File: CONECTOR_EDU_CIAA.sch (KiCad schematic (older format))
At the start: 2 parts

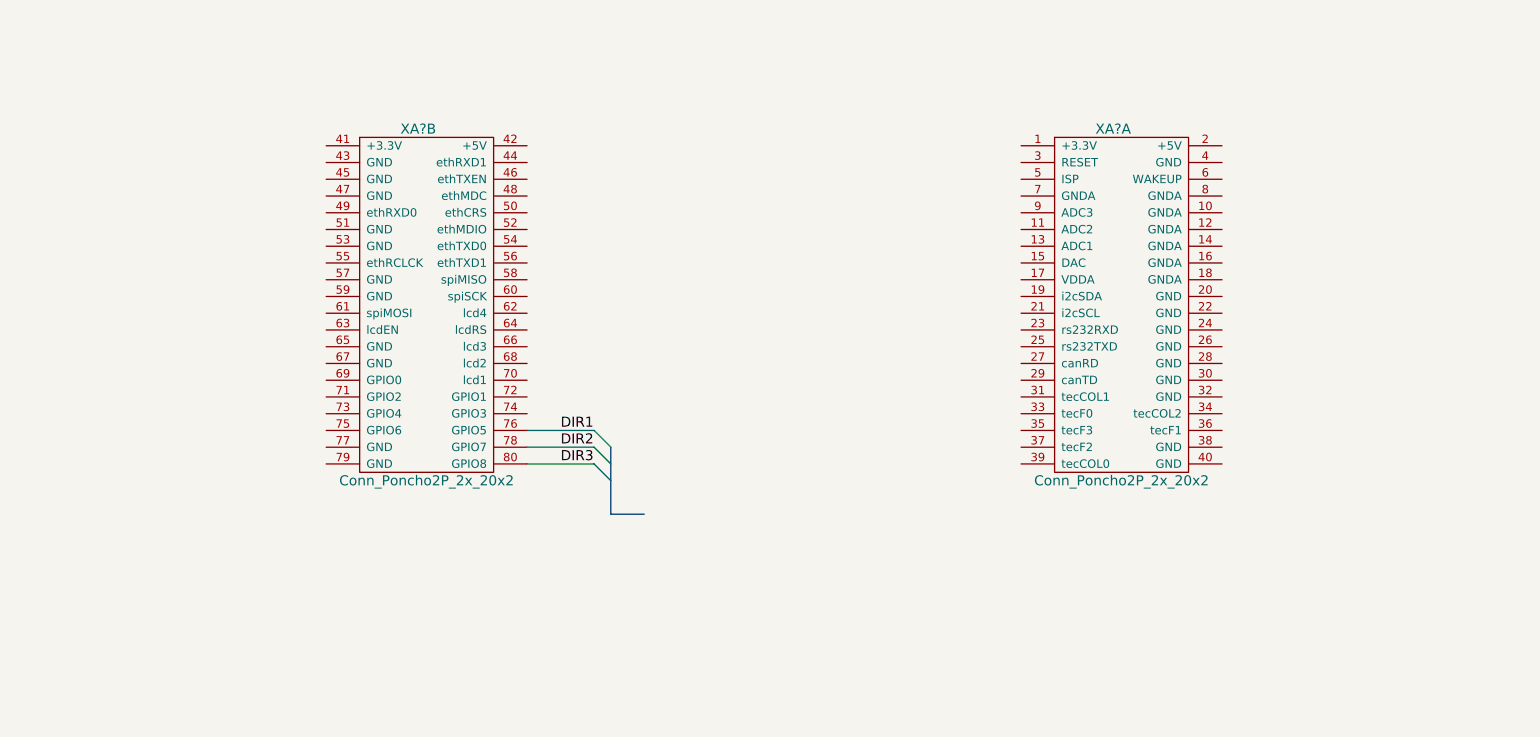
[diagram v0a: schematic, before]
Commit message: Adicion de documentacion
Creacion y adicion de componente A4988 en hoja POLOLUS_AXIS.sch, Avance parcialmente completo de  hoja POLOLUS_AXIS.sch
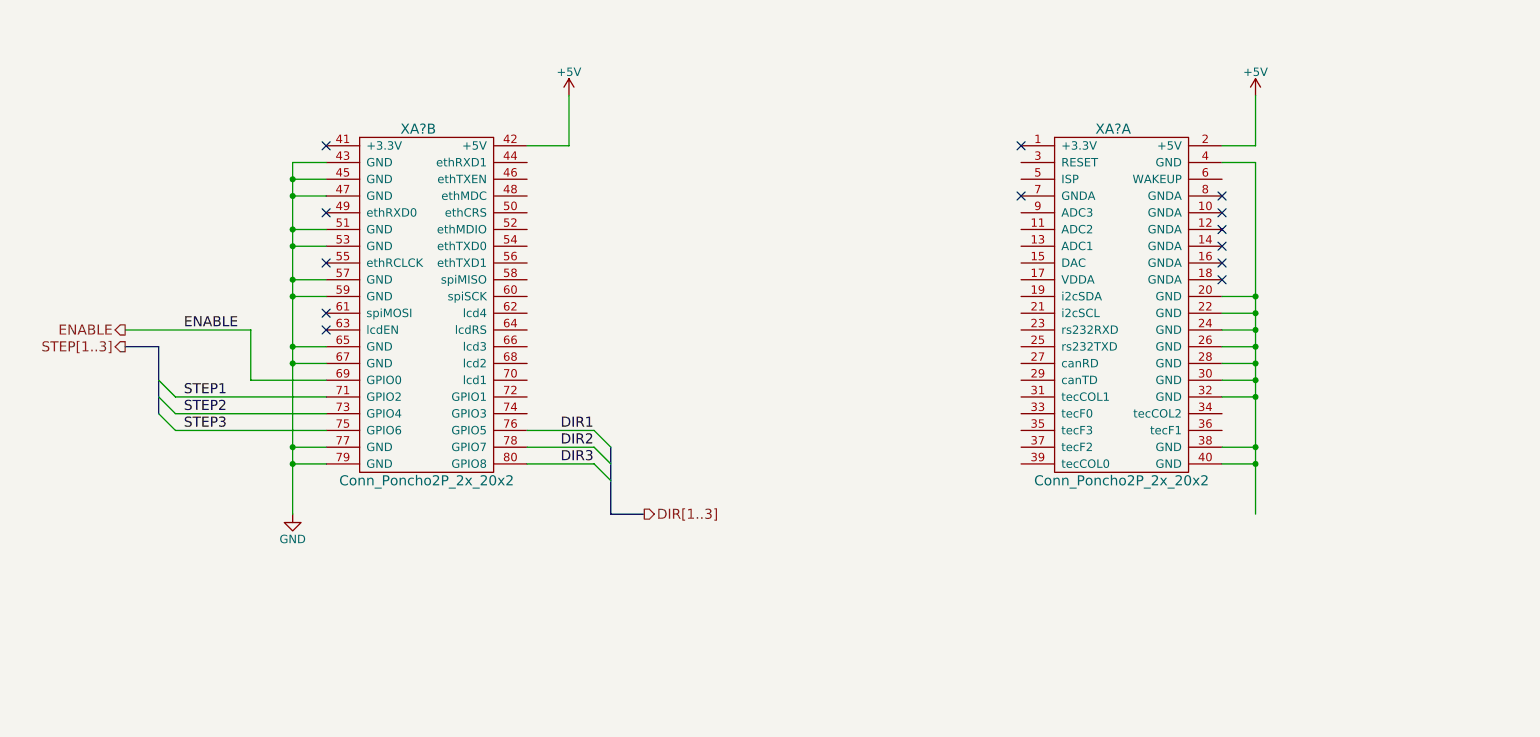
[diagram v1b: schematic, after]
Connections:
- net +5V: now reaches XA?.2 (+5V)
- net +5V: now also XA?.42 (+5V)
- net at XA?.20 (GND): now also XA?.22 (GND), XA?.24 (GND), XA?.26 (GND), XA?.28 (GND), XA?.30 (GND), XA?.32 (GND), XA?.38 (GND), XA?.4 (GND), XA?.40 (GND)
- net GND: now reaches XA?.43 (GND)
- net GND: now also XA?.45 (GND), XA?.47 (GND), XA?.51 (GND), XA?.53 (GND), XA?.57 (GND), XA?.59 (GND), XA?.65 (GND), XA?.67 (GND), XA?.77 (GND), XA?.79 (GND)
- net ENABLE: now reaches XA?.69 (GPIO0)
- net STEP1: now reaches XA?.71 (GPIO2)
- net STEP2: now reaches XA?.73 (GPIO4)
- net STEP3: now reaches XA?.75 (GPIO6)
- no-connect marks 0 -> 13
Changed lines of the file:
@@
 LIBS:Poncho_Esqueleto
 LIBS:Misc_Poncho_Grande
+LIBS:CNC_PONCHO_EDU_NXP-cache
 EELAYER 25 0
 EELAYER END
@@
 Text Label 4550 4300 0    60   ~ 0
 DIR3
+Text HLabel 5050 4600 2    60   Output ~ 0
+DIR[1..3]
+Wire Wire Line
+	3150 4300 2950 4300
+Wire Wire Line
+	3150 4200 2950 4200
+Wire Wire Line
+	3150 4100 2250 4100
+Wire Wire Line
+	2250 4000 3150 4000
+Wire Wire Line
+	3150 3900 2250 3900
+Entry Wire Line
+	2150 3800 2250 3900
+Entry Wire Line
+	2150 3900 2250 4000
+Entry Wire Line
+	2150 4000 2250 4100
+Wire Bus Line
+	2150 3600 2150 4000
+Wire Bus Line
+	2150 3600 1950 3600
+Text HLabel 1950 3600 0    60   Output ~ 0
+STEP[1..3]
+Text Label 2300 3900 0    60   ~ 0
+STEP1
+Text Label 2300 4000 0    60   ~ 0
+STEP2
+Text Label 2300 4100 0    60   ~ 0
+STEP3
+Wire Wire Line
+	2700 3800 3150 3800
+Text HLabel 1950 3500 0    60   Output ~ 0
+ENABLE
+Wire Wire Line
+	1950 3500 2700 3500
+Wire Wire Line
+	2700 3500 2700 3800
+Wire Wire Line
+	3150 3700 2950 3700
+Wire Wire Line
+	2950 2500 2950 4600
+Connection ~ 2950 4200
+Connection ~ 2950 4300
+Connection ~ 2950 3700
+Wire Wire Line
+	2950 2500 3150 2500
+Wire Wire Line
+	3150 2600 2950 2600
+Connection ~ 2950 2600
+Wire Wire Line
+	3150 2700 2950 2700
+Connection ~ 2950 2700
+Wire Wire Line
+	3150 2900 2950 2900
+Connection ~ 2950 2900
+Wire Wire Line
+	3150 3000 2950 3000
+Connection ~ 2950 3000
+Wire Wire Line
+	3150 3200 2950 3200
+Connection ~ 2950 3200
+Wire Wire Line
+	3150 3300 2950 3300
+Connection ~ 2950 3300
+Wire Wire Line
+	3150 3600 2950 3600
+Connection ~ 2950 3600
+NoConn ~ 3150 3500
+NoConn ~ 3150 3400
+NoConn ~ 3150 3100
+NoConn ~ 3150 2800
+NoConn ~ 3150 2400
+$Comp
+L GND #PWR01
+U 1 1 583A2490
+P 2950 4600
+F 0 "#PWR01" H 2950 4350 50  0001 C CNN
+F 1 "GND" H 2950 4450 50  0000 C CNN
+F 2 "" H 2950 4600 50  0000 C CNN
+F 3 "" H 2950 4600 50  0000 C CNN
+	1    2950 4600
+	1    0    0    -1
+$EndComp
+NoConn ~ 8500 2700
+NoConn ~ 8500 2800
+NoConn ~ 8500 2900
+NoConn ~ 8500 3000
+NoConn ~ 8500 3100
+NoConn ~ 8500 3200
+NoConn ~ 7300 2700
+NoConn ~ 7300 2400
+Wire Wire Line
+	8700 2500 8700 4600
+Wire Wire Line
+	8700 4300 8500 4300
+Wire Wire Line
+	8500 4200 8700 4200
+Connection ~ 8700 4300
+Wire Wire Line
+	8700 2500 8500 2500
+Connection ~ 8700 4200
+Wire Wire Line
+	8500 3900 8700 3900
+Connection ~ 8700 3900
+Wire Wire Line
+	8500 3800 8700 3800
+Connection ~ 8700 3800
+Wire Wire Line
+	8500 3700 8700 3700
+Connection ~ 8700 3700
+Wire Wire Line
+	8500 3600 8700 3600
+Connection ~ 8700 3600
+Wire Wire Line
+	8500 3500 8700 3500
+Connection ~ 8700 3500
+Wire Wire Line
+	8500 3400 8700 3400
+Connection ~ 8700 3400
+Wire Wire Line
+	8500 3300 8700 3300
+Connection ~ 8700 3300
+$Comp
+L +5V #PWR02
+U 1 1 583A47F1
+P 4600 2100
+F 0 "#PWR02" H 4600 1950 50  0001 C CNN
+F 1 "+5V" H 4600 2240 50  0000 C CNN
+F 2 "" H 4600 2100 50  0000 C CNN
+F 3 "" H 4600 2100 50  0000 C CNN
+	1    4600 2100
+	1    0    0    -1
+$EndComp
+$Comp
+L +5V #PWR03
+U 1 1 583A485D
+P 8700 2100
+F 0 "#PWR03" H 8700 1950 50  0001 C CNN
+F 1 "+5V" H 8700 2240 50  0000 C CNN
+F 2 "" H 8700 2100 50  0000 C CNN
+F 3 "" H 8700 2100 50  0000 C CNN
+	1    8700 2100
+	1    0    0    -1
+$EndComp
+Wire Wire Line
+	8500 2400 8700 2400
+Wire Wire Line
+	8700 2400 8700 2100
+Wire Wire Line
+	4350 2400 4600 2400
+Wire Wire Line
+	4600 2400 4600 2100
+Text Label 2300 3500 0    60   ~ 0
+ENABLE
 $EndSCHEMATC

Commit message: Reorganizacion de carpetas y avance de esquematico
Creacion de componente LM2596. Hoja REGULADOR finalizada. Avance parcial en hoja CONECTOR_EDU_CIAA. Creacion de carpetas datasheet y doc. Adicion de hojas de datos de LM2596, A4988, MMBT2222A. Adicion de documentacion LICENCIA, README, Revisiones.
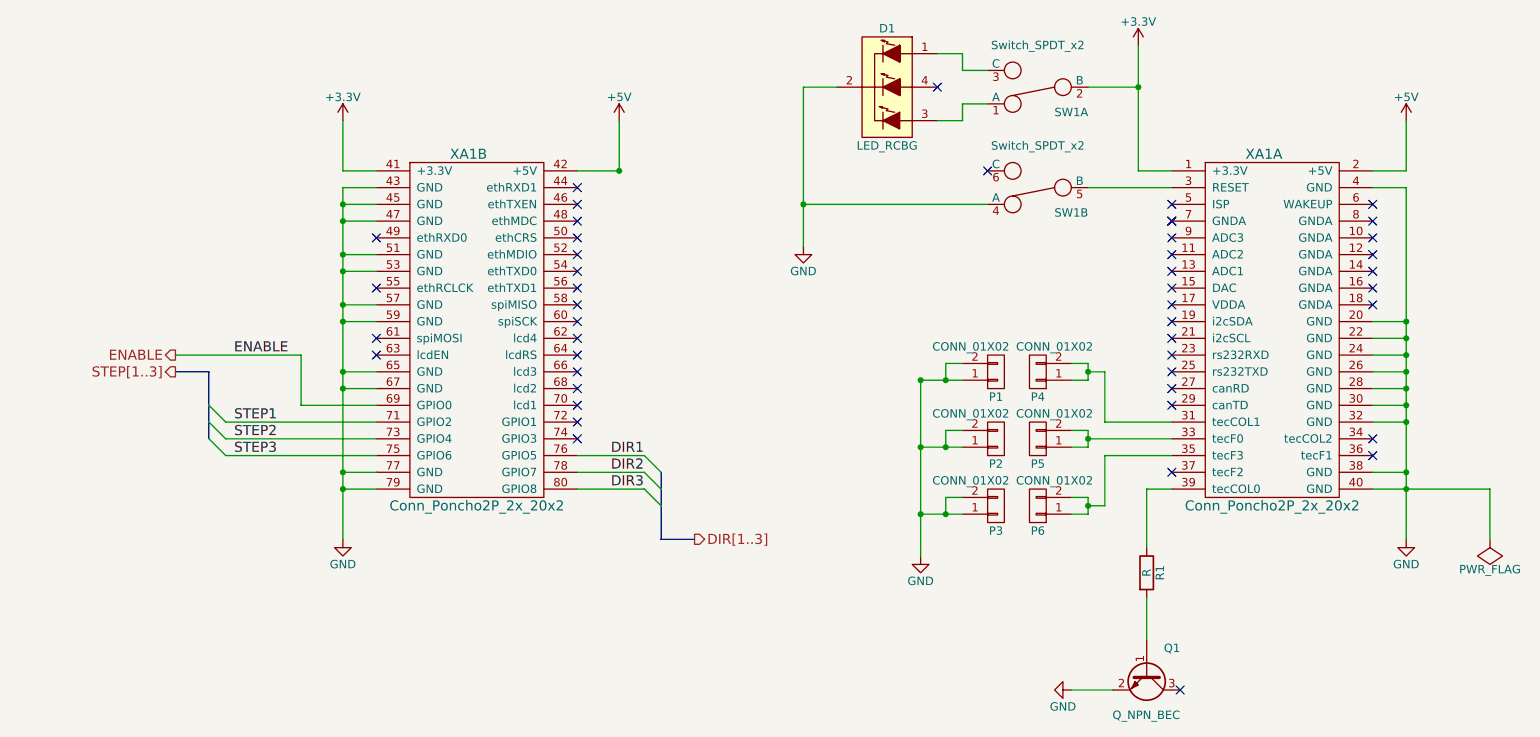
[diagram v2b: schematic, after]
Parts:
- added D1: LED_RCBG, symbol LED_RCBG
- added P1, P2, P3, P4, P5, P6: CONN_01X02, symbol CONN_01X02
- added Q1: Q_NPN_BEC, symbol Q_NPN_BEC
- added R1: R, symbol R
- added SW1: Switch_SPDT_x2, symbol Switch_SPDT_x2
- gave numbers to parts that had none: 1
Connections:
- net GND: now also XA1.20 (GND), XA1.22 (GND), XA1.24 (GND), XA1.26 (GND), XA1.28 (GND), XA1.30 (GND), XA1.32 (GND), XA1.38 (GND), XA1.4 (GND), XA1.40 (GND), D1.2 (COMMON_CATHODE), P1.1 (P1), P1.2 (P2), P2.1 (P1), P2.2 (P2), P3.1 (P1), P3.2 (P2), Q1.2 (E), SW1.4 (A)
- net +3V3: now reaches XA1.1 (+3.3V)
- net +3V3: now also XA1.41 (+3.3V), SW1.2 (B)
- net at XA1.3 (RESET): now also SW1.5 (B)
- net at XA1.31 (tecCOL1): now also P4.1 (P1), P4.2 (P2)
- net at XA1.33 (tecF0): now also P5.1 (P1), P5.2 (P2)
- net at XA1.35 (tecF3): now also P6.1 (P1), P6.2 (P2)
- net at XA1.39 (tecCOL0): now also R1.1
- new net: D1.3 (BLUE_ANODE), SW1.1 (A)
- new net: D1.1 (RED_ANODE), SW1.3 (C)
- new net: Q1.1 (B), R1.2
- no-connect marks 13 -> 47
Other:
- moved on the sheet: XA1A, XA1B
